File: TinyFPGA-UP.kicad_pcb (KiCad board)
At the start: 2 copper layers, 17.8 x 35.6 mm, 35 parts, among them J1 Conn_01x14, J2 Conn_01x14, J3 USB_B_Micro, J4 Conn_02x08_Odd_Even, J5 Conn_02x03_Odd_Even, SW1 SW_Push, U1 iCE40-UP5K-SG48, U2 MIC5504-3.3, U3 DSC6001CI2A, U4 MIC5365-1.2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

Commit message: Update routing
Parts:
- added C10: 100nF, Capacitor_SMD:C_0402_1005Metric, F.Cu at (145.8, 116.1)
- added C11: 100nF, Capacitor_SMD:C_0402_1005Metric, F.Cu at (156.2, 114.5)
- added C12: 100nF, Capacitor_SMD:C_0402_1005Metric, F.Cu at (156.0, 124.1)
- added C13: 100nF, Capacitor_SMD:C_0402_1005Metric, F.Cu at (146.2, 112.9)
- added C14: 100nF, Capacitor_SMD:C_0402_1005Metric, F.Cu at (153.6, 111.2)
- added C15: 100nF, Capacitor_SMD:C_0402_1005Metric, F.Cu at (157.1, 114.5)
- added C16: 100nF, Capacitor_SMD:C_0402_1005Metric, F.Cu at (146.4, 121.1)
- added C18: 100nF, Capacitor_SMD:C_0402_1005Metric, F.Cu at (146.4, 124.4)
- added C19: 100nF, Capacitor_SMD:C_0402_1005Metric, F.Cu at (152.2, 108.8)
- added C20: 100nF, Capacitor_SMD:C_0402_1005Metric, F.Cu at (149.8, 105.8)
- added C21: 100nF, Capacitor_SMD:C_0402_1005Metric, F.Cu at (156.0, 127.0)
- added C22: 100nF, Capacitor_SMD:C_0402_1005Metric, F.Cu at (156.0, 126.0)
- added C6: 10uF, Capacitor_SMD:C_0402_1005Metric, F.Cu at (157.1, 117.0)
- added C7: 100nF, Capacitor_SMD:C_0402_1005Metric, F.Cu at (155.1, 120.7)
- added C9: 100nF, Capacitor_SMD:C_0402_1005Metric, F.Cu at (154.6, 111.2)
- added D4: RGB, DRA818:LTST-C19HE1WT, F.Cu at (155.7, 130.5)
- added R11: 0, Resistor_SMD:R_0402_1005Metric, F.Cu at (145.7, 105.7)
- added R12: 100, Resistor_SMD:R_0402_1005Metric, F.Cu at (156.2, 128.6)
- added R13: 100, Resistor_SMD:R_0402_1005Metric, F.Cu at (155.3, 128.6)
- added R14: 100, Resistor_SMD:R_0402_1005Metric, F.Cu at (154.4, 128.6)
- added R15: DNP, Resistor_SMD:R_0402_1005Metric, F.Cu at (146.3, 130.8)
- added R16: 0, Resistor_SMD:R_0402_1005Metric, B.Cu at (155.0, 121.9)
- added R17: 0, Resistor_SMD:R_0402_1005Metric, B.Cu at (149.9, 121.9)
- added REF**: OSHW-Logo2_7.3x6mm_SilkScreen, Symbol:OSHW-Logo2_7.3x6mm_SilkScreen, B.Cu at (151.6, 109.4)
- R8: value 270 -> 2.2k
- moved C5 17.8 mm to (147.2, 107.1), turned to 180 degrees
- moved C8 14.2 mm to (149.7, 127.5), turned to 0 degrees
- moved R6 6.82 mm to (147.7, 130.3)
- moved R5 6.12 mm to (156.0, 125.1), turned to 180 degrees
- moved R10 1.34 mm to (156.0, 123.2)
- moved R7 0.90 mm to (147.2, 127.5), turned to 180 degrees
- moved D3 0.72 mm to (156.6, 120.8), turned to 270 degrees
- moved R8 0.50 mm to (146.7, 105.7), turned to 90 degrees
- moved R4 0.13 mm to (156.1, 117.0)
- turned D1 to 270 degrees
- turned D2 to 270 degrees
- turned R9 to 90 degrees
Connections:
- D1 pad 1: Net-(D1-Pad1) -> GND
- D1 pad 2: +3V3 -> Net-(D1-Pad2)
- D2 pad 1: Net-(D2-Pad1) -> GND
- D2 pad 2: LED -> Net-(D2-Pad2)
- J3 pad 4: (no net) -> Net-(J3-Pad4)
- J4 pad 1: (no net) -> RGB0
- J4 pad 2: (no net) -> RGB2
- J4 pad 5: (no net) -> RGB1
- J4 pad 6: (no net) -> Net-(J4-Pad6)
- J4 pad 7: (no net) -> 29B
- J4 pad 8: (no net) -> 31B
- R8 pad 1: Net-(D1-Pad1) -> +3V3
- R8 pad 2: GND -> Net-(D1-Pad2)
- R9 pad 1: Net-(D2-Pad1) -> LED
- R9 pad 2: GND -> Net-(D2-Pad2)
- U1 pad 18: (no net) -> 31B
- U1 pad 19: (no net) -> 29B
- U1 pad 39: (no net) -> RGB0
- U1 pad 40: (no net) -> RGB1
- U1 pad 41: (no net) -> RGB2
- U1 pad 7: (no net) -> CDONE
- U2 pad 4: (no net) -> Net-(U2-Pad4)
- U4 pad 4: (no net) -> Net-(U4-Pad4)
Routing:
- net GND: track 1.65 -> 57.2 mm, vias 1 -> 27
- net RGB1: track 0.00 -> 32.5 mm, vias 0 -> 2
- net +1V2: track 3.77 -> 30.8 mm, vias 1 -> 4
- net RGB0: track 0.00 -> 25.8 mm, vias 0 -> 2
- net CDONE: track 0.00 -> 24.8 mm, vias 0 -> 2
- net RGB2: track 0.00 -> 24.1 mm, vias 0 -> 2
- net +3V3: track 32.0 -> 50.9 mm, vias 5 -> 10
- net (no net): track 17.8 -> 0.00 mm, vias 2 -> 0
- net WP: track 9.84 -> 17.6 mm
- net 29B: track 0.00 -> 6.06 mm, vias 0 -> 1
- net 31B: track 0.00 -> 4.33 mm, vias 0 -> 1
- net Net-(D3-Pad1): track 0.00 -> 2.75 mm
- net Net-(D1-Pad2): track 0.00 -> 2.58 mm
- net Net-(D4-Pad1): track 0.00 -> 2.54 mm
- net LED: track 27.4 -> 29.9 mm
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- added copper zone on In2.Cu, net +3V3
- added copper zone on In1.Cu, net GND
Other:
- copper layers 2 -> 4
- board text added: "1"
- board text added: "1.2v"
- board text added: "10"
- board text added: "11"
- board text added: "12"
- board text added: "13"
- board text added: "14"
- board text added: "15"
- board text added: "16"
- board text added: "17"
- board text added: "18"
- board text added: "19"
- board text added: "2"
- board text added: "20"
- board text added: "21"
- board text added: "22"
- board text added: "23"
- board text added: "24"
- board text added: "27"
- board text added: "28"
- board text added: "3"
- board text added: "3.3v"
- board text added: "31"
- board text added: "4"
- board text added: "5"
- board text added: "6"
- board text added: "7"
- board text added: "8"
- board text added: "9"
- board text added: "CLK"
- board text added: "DinyFPGA UP"
- board text added: "G"
- board text added: "GND"
- board text added: "HB9GPC"
- board text added: "HLD"
- board text added: "LD0"
- board text added: "LD1"
- board text added: "LD2"
- board text added: "LED"
- board text added: "NC"
- board text added: "PU"
- board text added: "RST"
- board text added: "SCK"
- board text added: "SDI"
- board text added: "SDO"
- board text added: "SS"
- board text added: "U+"
- board text added: "U-"
- board text added: "Vin"
- board text added: "WP"
- board text added: "rev. A"

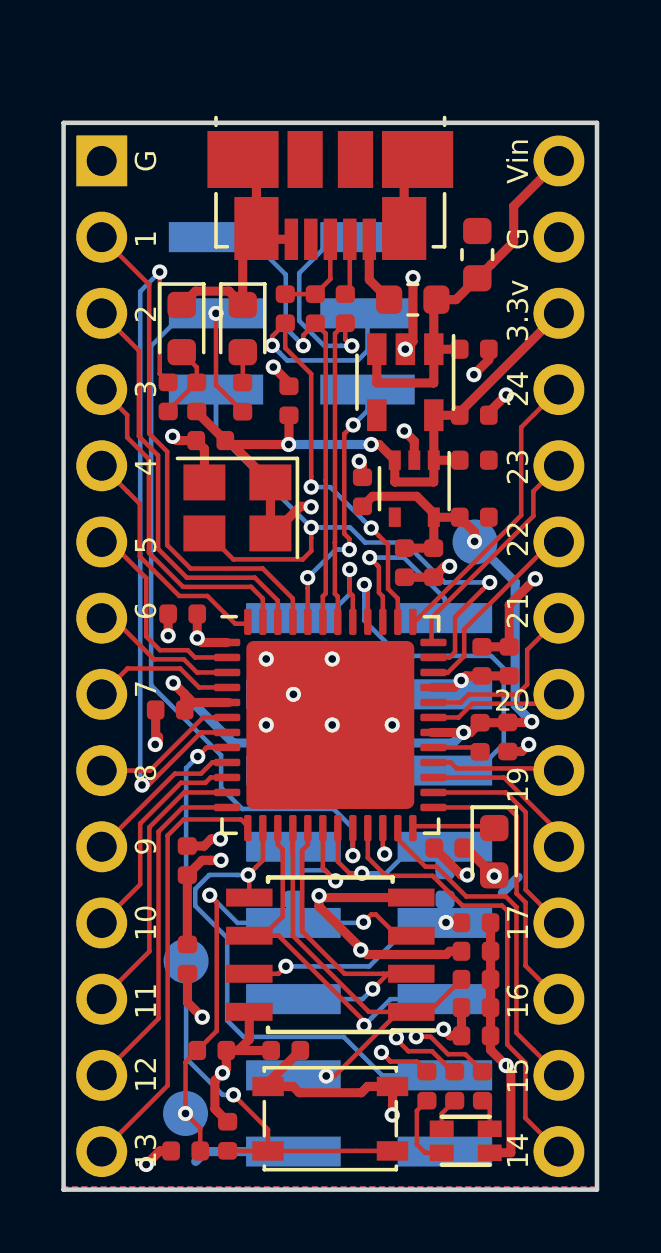
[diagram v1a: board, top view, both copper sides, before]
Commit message: Make LED, WP, HLC compatible
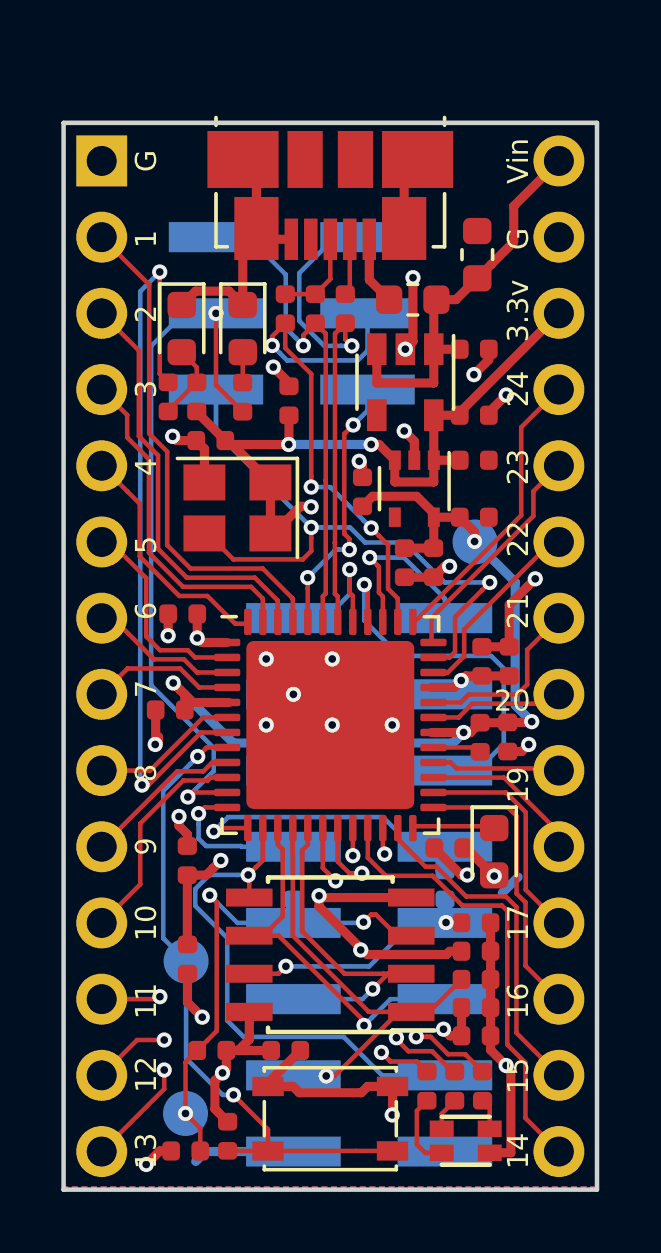
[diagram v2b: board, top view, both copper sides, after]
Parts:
- removed REF**: OSHW-Logo2_7.3x6mm_SilkScreen, Symbol:OSHW-Logo2_7.3x6mm_SilkScreen
- C10, C11, C12, C22: value 100nF -> 10nF
- C13, C19, C20, C21: value 100nF -> 1uF
- J4: value Conn_02x08_Odd_Even -> Conn_02x08
- J5: value Conn_02x03_Odd_Even -> Conn_02x03
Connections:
- J1 pad 12: 20A -> 25B
- J1 pad 13: 22A -> 29B
- J1 pad 14: 24A -> 31B
- J4 pad 7: 29B -> 24A
- J4 pad 8: 31B -> 22A
- R16 pad 1: 29B -> 24A
- R17 pad 1: 31B -> 22A
- U1 pad 11: 20A -> LED
- U1 pad 20: LED -> 25B
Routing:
- net +3V3: track 50.9 -> 67.2 mm
- net 25B: track 0.00 -> 11.4 mm, vias 0 -> 2
- net 31B: track 4.33 -> 14.7 mm, vias 1 -> 2
- net 20A: track 9.52 -> 0.00 mm
- net 29B: track 6.06 -> 14.3 mm, vias 1 -> 2
- net 22A: track 11.6 -> 5.93 mm, vias 0 -> 1
- net LED: track 29.9 -> 25.0 mm
- net 24A: track 14.4 -> 10.3 mm, vias 0 -> 1
- net CRESET_B: track 21.3 -> 22.0 mm

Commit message: Adding plots
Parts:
- added REF**: OSHW-Logo2_7.3x6mm_SilkScreen, Symbol:OSHW-Logo2_7.3x6mm_SilkScreen, B.Cu at (151.5, 109.3)
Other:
- board text added: "TinyFPGA UP"
- board text removed: "DinyFPGA UP"
